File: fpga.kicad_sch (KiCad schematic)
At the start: 58 parts, among them J7 2X05, J8 61300411121, Q6 2N7002, U11 LIFCL-40-9BG256C, U17 SC18IS602BIPW, U18 W25Q32JVSSIQ, Y2 OSC40M-3.3_S5

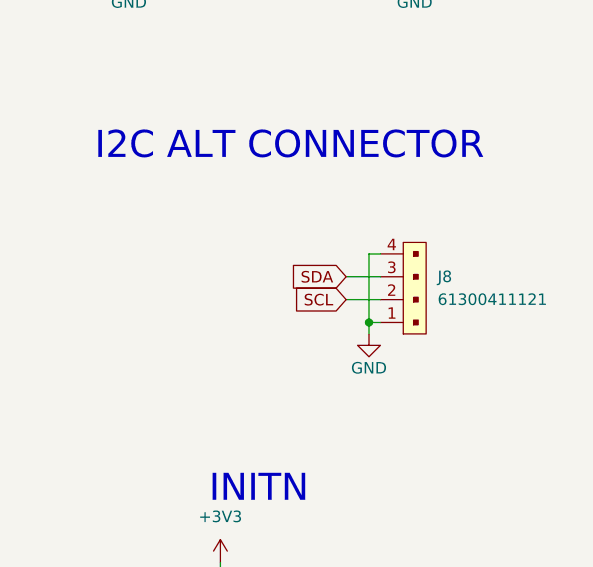
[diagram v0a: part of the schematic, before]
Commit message: Switched voltages to support DDR3 and RPC memories
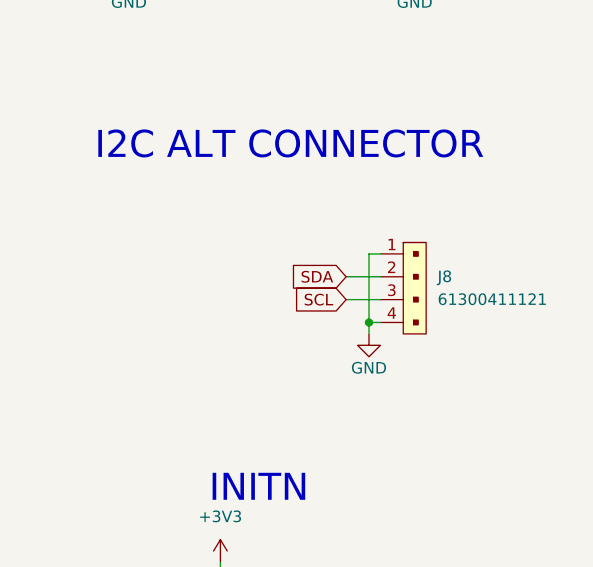
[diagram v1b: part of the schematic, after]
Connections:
- net SCL: now also J8.3; no longer J8.2
- net SDA: now also J8.2; no longer J8.3
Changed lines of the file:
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@@
     (pin "1")
   )
-  (symbol (lib_id "antmicroRectangularConnectorsHeadersMalePins:61300411121") (at 383.54 175.26 90) (unit 1)
+  (symbol (lib_id "antmicroRectangularConnectorsHeadersMalePins:61300411121") (at 383.54 167.64 90) (mirror x) (unit 1)
     (in_bom yes) (on_board yes) (fields_autoplaced)
     (property "Reference" "J8" (id 0) (at 386.08 170.1799 90)
@@
       (effects (font (size 1.27 1.27)) (justify right))
     )
-    (property "Footprint" "antmicro-footprints:PinHeader_1x4_P2.54mm_Drill1.02mm" (id 2) (at 378.46 170.18 0)
+    (property "Footprint" "antmicro-footprints:PinHeader_1x4_P2.54mm_Drill1.02mm" (id 2) (at 378.46 172.72 0)
       (effects (font (size 1.524 1.524)) (justify left) hide)
     )
-    (property "Datasheet" "" (id 3) (at 375.92 170.18 0)
+    (property "Datasheet" "" (id 3) (at 375.92 172.72 0)
       (effects (font (size 1.524 1.524)) (justify left) hide)
     )
-    (property "MPN" "61300411121" (id 4) (at 370.84 170.18 0)
+    (property "MPN" "61300411121" (id 4) (at 370.84 172.72 0)
       (effects (font (size 1.524 1.524)) (justify left) hide)
     )
-    (property "Manufacturer" "Wurth Electronics Inc." (id 5) (at 355.6 170.18 0)
+    (property "Manufacturer" "Wurth Electronics Inc." (id 5) (at 355.6 172.72 0)
       (effects (font (size 1.524 1.524)) (justify left) hide)
     )

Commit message: Placed components
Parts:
- C75: renamed from C81; value C_100n_0603 -> C_100n_0402; footprint crosslink-nx-video-converter-footprints:0603-cap -> antmicro-footprints:0402-cap; symbol crosslink-nx-video-converter:C_100n_0603 -> antmicroCapacitors0402:C_100n_0402; MPN 0603YC104KAZ2A -> GRM155R61H104KE14D; Manufacturer AVX -> Murata
- C79: renamed from C82; value C_100n_0603 -> C_100n_0402; footprint crosslink-nx-video-converter-footprints:0603-cap -> antmicro-footprints:0402-cap; symbol crosslink-nx-video-converter:C_100n_0603 -> antmicroCapacitors0402:C_100n_0402; DNP DNP -> (none); MPN 0603YC104KAZ2A -> GRM155R61H104KE14D; Manufacturer AVX -> Murata; now in the parts list
- C80: renamed from C83; value C_100n_0603 -> C_100n_0402; footprint crosslink-nx-video-converter-footprints:0603-cap -> antmicro-footprints:0402-cap; symbol crosslink-nx-video-converter:C_100n_0603 -> antmicroCapacitors0402:C_100n_0402; MPN 0603YC104KAZ2A -> GRM155R61H104KE14D; Manufacturer AVX -> Murata
- C81: renamed from C84; value C_100n_0603 -> C_100n_0402; footprint crosslink-nx-video-converter-footprints:0603-cap -> antmicro-footprints:0402-cap; symbol crosslink-nx-video-converter:C_100n_0603 -> antmicroCapacitors0402:C_100n_0402; MPN 0603YC104KAZ2A -> GRM155R61H104KE14D; Manufacturer AVX -> Murata
- C82: renamed from C85; value C_100n_0603 -> C_100n_0402; footprint crosslink-nx-video-converter-footprints:0603-cap -> antmicro-footprints:0402-cap; symbol crosslink-nx-video-converter:C_100n_0603 -> antmicroCapacitors0402:C_100n_0402; MPN 0603YC104KAZ2A -> GRM155R61H104KE14D; Manufacturer AVX -> Murata
- R39: renamed from R65; value R_0R_0603 -> R_0R_0402; footprint crosslink-nx-video-converter-footprints:0603-res -> antmicro-footprints:0402-res; symbol crosslink-nx-video-converter:R_0R_0603 -> antmicroResistors0402:R_0R_0402; DNP DNP -> (none); MPN CR0603-J/-000ELF -> ERJ2GE0R00X; Manufacturer BOURNS -> PANASONIC; now in the parts list
- R58: renamed from R66; value R_0R_0603 -> R_0R_0402; footprint crosslink-nx-video-converter-footprints:0603-res -> antmicro-footprints:0402-res; symbol crosslink-nx-video-converter:R_0R_0603 -> antmicroResistors0402:R_0R_0402; MPN CR0603-J/-000ELF -> ERJ2GE0R00X; Manufacturer BOURNS -> PANASONIC
- R65: renamed from R67; value R_0R_0603 -> R_0R_0402; footprint crosslink-nx-video-converter-footprints:0603-res -> antmicro-footprints:0402-res; symbol crosslink-nx-video-converter:R_0R_0603 -> antmicroResistors0402:R_0R_0402; MPN CR0603-J/-000ELF -> ERJ2GE0R00X; Manufacturer BOURNS -> PANASONIC
- R66: renamed from R69; value R_0R_0603 -> R_0R_0402; footprint crosslink-nx-video-converter-footprints:0603-res -> antmicro-footprints:0402-res; symbol crosslink-nx-video-converter:R_0R_0603 -> antmicroResistors0402:R_0R_0402; MPN CR0603-J/-000ELF -> ERJ2GE0R00X; Manufacturer BOURNS -> PANASONIC
- R67: renamed from R71; value R_0R_0603 -> R_0R_0402; footprint crosslink-nx-video-converter-footprints:0603-res -> antmicro-footprints:0402-res; symbol crosslink-nx-video-converter:R_0R_0603 -> antmicroResistors0402:R_0R_0402; MPN CR0603-J/-000ELF -> ERJ2GE0R00X; Manufacturer BOURNS -> PANASONIC
- R68, R81, R91: value R_10k_0603 -> R_10k_0402; footprint crosslink-nx-video-converter-footprints:0603-res -> antmicro-footprints:0402-res; symbol crosslink-nx-video-converter:R_10k_0603 -> antmicroResistors0402:R_10k_0402; MPN CR0603-JW-103ELF -> CRCW040210K0FKEDHP; Manufacturer BOURNS -> VISHAY
- R69: renamed from R73; value R_0R_0603 -> R_0R_0402; footprint crosslink-nx-video-converter-footprints:0603-res -> antmicro-footprints:0402-res; symbol crosslink-nx-video-converter:R_0R_0603 -> antmicroResistors0402:R_0R_0402; MPN CR0603-J/-000ELF -> ERJ2GE0R00X; Manufacturer BOURNS -> PANASONIC
- R70, R72, R84: value R_100R_0603 -> R_100R_0402; footprint crosslink-nx-video-converter-footprints:0603-res -> antmicro-footprints:0402-res; symbol crosslink-nx-video-converter:R_100R_0603 -> antmicroResistors0402:R_100R_0402; MPN MC0063W06035100R -> CR0402-FX-1000GLF; Manufacturer MULTICOMP -> BOURNS
- R71: renamed from R74; value R_0R_0603 -> R_0R_0402; footprint crosslink-nx-video-converter-footprints:0603-res -> antmicro-footprints:0402-res; symbol crosslink-nx-video-converter:R_0R_0603 -> antmicroResistors0402:R_0R_0402; MPN CR0603-J/-000ELF -> ERJ2GE0R00X; Manufacturer BOURNS -> PANASONIC
- R73: renamed from R75; value R_0R_0603 -> R_0R_0402; footprint crosslink-nx-video-converter-footprints:0603-res -> antmicro-footprints:0402-res; symbol crosslink-nx-video-converter:R_0R_0603 -> antmicroResistors0402:R_0R_0402; MPN CR0603-J/-000ELF -> ERJ2GE0R00X; Manufacturer BOURNS -> PANASONIC
- R74: renamed from R76; value R_0R_0603 -> R_0R_0402; footprint crosslink-nx-video-converter-footprints:0603-res -> antmicro-footprints:0402-res; symbol crosslink-nx-video-converter:R_0R_0603 -> antmicroResistors0402:R_0R_0402; MPN CR0603-J/-000ELF -> ERJ2GE0R00X; Manufacturer BOURNS -> PANASONIC
- R75: renamed from R77; value R_0R_0603 -> R_0R_0402; footprint crosslink-nx-video-converter-footprints:0603-res -> antmicro-footprints:0402-res; symbol crosslink-nx-video-converter:R_0R_0603 -> antmicroResistors0402:R_0R_0402; MPN CR0603-J/-000ELF -> ERJ2GE0R00X; Manufacturer BOURNS -> PANASONIC
- R76: renamed from R78; value R_0R_0603 -> R_0R_0402; footprint crosslink-nx-video-converter-footprints:0603-res -> antmicro-footprints:0402-res; symbol crosslink-nx-video-converter:R_0R_0603 -> antmicroResistors0402:R_0R_0402; MPN CR0603-J/-000ELF -> ERJ2GE0R00X; Manufacturer BOURNS -> PANASONIC
- R77: renamed from R80; value R_0R_0603 -> R_0R_0402; footprint crosslink-nx-video-converter-footprints:0603-res -> antmicro-footprints:0402-res; symbol crosslink-nx-video-converter:R_0R_0603 -> antmicroResistors0402:R_0R_0402; MPN CR0603-J/-000ELF -> ERJ2GE0R00X; Manufacturer BOURNS -> PANASONIC
- R78: renamed from R82; value R_0R_0603 -> R_0R_0402; footprint crosslink-nx-video-converter-footprints:0603-res -> antmicro-footprints:0402-res; symbol crosslink-nx-video-converter:R_0R_0603 -> antmicroResistors0402:R_0R_0402; MPN CR0603-J/-000ELF -> ERJ2GE0R00X; Manufacturer BOURNS -> PANASONIC
- R79: value R_1k_0603 -> R_1k_0402; footprint crosslink-nx-video-converter-footprints:0603-res -> antmicro-footprints:0402-res; symbol crosslink-nx-video-converter:R_1k_0603 -> antmicroResistors0402:R_1k_0402; MPN CR0603-JW-102ELF -> CR0402-FX-1001GLF
- R80: renamed from R85; value R_0R_0603 -> R_0R_0402; footprint crosslink-nx-video-converter-footprints:0603-res -> antmicro-footprints:0402-res; symbol crosslink-nx-video-converter:R_0R_0603 -> antmicroResistors0402:R_0R_0402; MPN CR0603-J/-000ELF -> ERJ2GE0R00X; Manufacturer BOURNS -> PANASONIC
- R82: renamed from R86; value R_0R_0603 -> R_0R_0402; footprint crosslink-nx-video-converter-footprints:0603-res -> antmicro-footprints:0402-res; symbol crosslink-nx-video-converter:R_0R_0603 -> antmicroResistors0402:R_0R_0402; MPN CR0603-J/-000ELF -> ERJ2GE0R00X; Manufacturer BOURNS -> PANASONIC
- R83, R87, R90: value R_4k7_0603 -> R_4k7_0402; footprint crosslink-nx-video-converter-footprints:0603-res -> antmicro-footprints:0402-res; symbol crosslink-nx-video-converter:R_4k7_0603 -> antmicroResistors0402:R_4k7_0402; MPN CR0603-FX-4701ELF -> MCS04020C4701FE000; Manufacturer BOURNS -> VISHAY
- R85: renamed from R88; value R_0R_0603 -> R_0R_0402; footprint crosslink-nx-video-converter-footprints:0603-res -> antmicro-footprints:0402-res; symbol crosslink-nx-video-converter:R_0R_0603 -> antmicroResistors0402:R_0R_0402; MPN CR0603-J/-000ELF -> ERJ2GE0R00X; Manufacturer BOURNS -> PANASONIC
- R86: renamed from R92; value R_0R_0603 -> R_0R_0402; footprint crosslink-nx-video-converter-footprints:0603-res -> antmicro-footprints:0402-res; symbol crosslink-nx-video-converter:R_0R_0603 -> antmicroResistors0402:R_0R_0402; MPN CR0603-J/-000ELF -> ERJ2GE0R00X; Manufacturer BOURNS -> PANASONIC
- R88: renamed from R94; value R_0R_0603 -> R_0R_0402; footprint crosslink-nx-video-converter-footprints:0603-res -> antmicro-footprints:0402-res; symbol crosslink-nx-video-converter:R_0R_0603 -> antmicroResistors0402:R_0R_0402; MPN CR0603-J/-000ELF -> ERJ2GE0R00X; Manufacturer BOURNS -> PANASONIC
- R89, R93: value R_2k2_0603 -> R_2k2_0402; footprint crosslink-nx-video-converter-footprints:0603-res -> antmicro-footprints:0402-res; symbol crosslink-nx-video-converter:R_2k2_0603 -> antmicroResistors0402:R_2k2_0402; MPN MCMR06X2201FTL -> RC0402FR-072K2L; Manufacturer MULTICOMP -> YAGEO
- R92: renamed from R95; value R_0R_0603 -> R_0R_0402; footprint crosslink-nx-video-converter-footprints:0603-res -> antmicro-footprints:0402-res; symbol crosslink-nx-video-converter:R_0R_0603 -> antmicroResistors0402:R_0R_0402; MPN CR0603-J/-000ELF -> ERJ2GE0R00X; Manufacturer BOURNS -> PANASONIC
- R94: renamed from R96; value R_0R_0603 -> R_0R_0402; footprint crosslink-nx-video-converter-footprints:0603-res -> antmicro-footprints:0402-res; symbol crosslink-nx-video-converter:R_0R_0603 -> antmicroResistors0402:R_0R_0402; MPN CR0603-J/-000ELF -> ERJ2GE0R00X; Manufacturer BOURNS -> PANASONIC
- R95: renamed from R97; value R_0R_0603 -> R_0R_0402; footprint crosslink-nx-video-converter-footprints:0603-res -> antmicro-footprints:0402-res; symbol crosslink-nx-video-converter:R_0R_0603 -> antmicroResistors0402:R_0R_0402; MPN CR0603-J/-000ELF -> ERJ2GE0R00X; Manufacturer BOURNS -> PANASONIC
- R96: renamed from R98; value R_0R_0603 -> R_0R_0402; footprint crosslink-nx-video-converter-footprints:0603-res -> antmicro-footprints:0402-res; symbol crosslink-nx-video-converter:R_0R_0603 -> antmicroResistors0402:R_0R_0402; MPN CR0603-J/-000ELF -> ERJ2GE0R00X; Manufacturer BOURNS -> PANASONIC
- R97: renamed from R99; value R_10k_0603 -> R_10k_0402; footprint crosslink-nx-video-converter-footprints:0603-res -> antmicro-footprints:0402-res; symbol crosslink-nx-video-converter:R_10k_0603 -> antmicroResistors0402:R_10k_0402; MPN CR0603-JW-103ELF -> CRCW040210K0FKEDHP; Manufacturer BOURNS -> VISHAY
- TP15: renamed from TP16; value TP -> TP_SMD_0_75MM; footprint crosslink-nx-video-converter-footprints:TP-R-1.5 -> antmicro-footprints:Testpoint_smd_0_75mm; symbol crosslink-nx-video-converter:TP -> antmicroTestPoints:TP_SMD_0_75MM
- TP16: renamed from TP17; value TP -> TP_SMD_0_75MM; footprint crosslink-nx-video-converter-footprints:TP-R-1.5 -> antmicro-footprints:Testpoint_smd_0_75mm; symbol crosslink-nx-video-converter:TP -> antmicroTestPoints:TP_SMD_0_75MM
- TP17: renamed from TP18; value TP -> TP_SMD_0_75MM; footprint crosslink-nx-video-converter-footprints:TP-R-1.5 -> antmicro-footprints:Testpoint_smd_0_75mm; symbol crosslink-nx-video-converter:TP -> antmicroTestPoints:TP_SMD_0_75MM
- TP18: renamed from TP19; value TP -> TP_SMD_0_75MM; footprint crosslink-nx-video-converter-footprints:TP-R-1.5 -> antmicro-footprints:Testpoint_smd_0_75mm; symbol crosslink-nx-video-converter:TP -> antmicroTestPoints:TP_SMD_0_75MM
- TP19: renamed from TP20; value TP -> TP_SMD_0_75MM; footprint crosslink-nx-video-converter-footprints:TP-R-1.5 -> antmicro-footprints:Testpoint_smd_0_75mm; symbol crosslink-nx-video-converter:TP -> antmicroTestPoints:TP_SMD_0_75MM
- TP20: renamed from TP21; value TP -> TP_SMD_0_75MM; footprint crosslink-nx-video-converter-footprints:TP-R-1.5 -> antmicro-footprints:Testpoint_smd_0_75mm; symbol crosslink-nx-video-converter:TP -> antmicroTestPoints:TP_SMD_0_75MM
- TP21: renamed from TP22; value TP -> TP_SMD_0_75MM; footprint crosslink-nx-video-converter-footprints:TP-R-1.5 -> antmicro-footprints:Testpoint_smd_0_75mm; symbol crosslink-nx-video-converter:TP -> antmicroTestPoints:TP_SMD_0_75MM
- TP22: renamed from TP23; value TP -> TP_SMD_0_75MM; footprint crosslink-nx-video-converter-footprints:TP-R-1.5 -> antmicro-footprints:Testpoint_smd_0_75mm; symbol crosslink-nx-video-converter:TP -> antmicroTestPoints:TP_SMD_0_75MM

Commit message: Loclib
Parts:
- C75, C79, C80, C81, C82: footprint antmicro-footprints:0402-cap -> crosslink-nx-video-converter-footprints:0402-cap; symbol antmicroCapacitors0402:C_100n_0402 -> crosslink-nx-video-converter:C_100n_0402
- J8: footprint antmicro-footprints:PinHeader_1x4_P2.54mm_Drill1.02mm -> crosslink-nx-video-converter-footprints:PinHeader_1x4_P2.54mm_Drill1.02mm; symbol antmicroRectangularConnectorsHeadersMalePins:61300411121 -> crosslink-nx-video-converter:61300411121
- R39, R58, R65, R66, R67, R69, R71, R73, R74, R75, R76, R77, R78, R80, R82, R85, R86, R88, R92, R94, R95, R96: footprint antmicro-footprints:0402-res -> crosslink-nx-video-converter-footprints:0402-res; symbol antmicroResistors0402:R_0R_0402 -> crosslink-nx-video-converter:R_0R_0402
- R68, R81, R91, R97: footprint antmicro-footprints:0402-res -> crosslink-nx-video-converter-footprints:0402-res; symbol antmicroResistors0402:R_10k_0402 -> crosslink-nx-video-converter:R_10k_0402
- R70, R72, R84: footprint antmicro-footprints:0402-res -> crosslink-nx-video-converter-footprints:0402-res; symbol antmicroResistors0402:R_100R_0402 -> crosslink-nx-video-converter:R_100R_0402
- R79: footprint antmicro-footprints:0402-res -> crosslink-nx-video-converter-footprints:0402-res; symbol antmicroResistors0402:R_1k_0402 -> crosslink-nx-video-converter:R_1k_0402
- R83, R87, R90: footprint antmicro-footprints:0402-res -> crosslink-nx-video-converter-footprints:0402-res; symbol antmicroResistors0402:R_4k7_0402 -> crosslink-nx-video-converter:R_4k7_0402
- R89, R93: footprint antmicro-footprints:0402-res -> crosslink-nx-video-converter-footprints:0402-res; symbol antmicroResistors0402:R_2k2_0402 -> crosslink-nx-video-converter:R_2k2_0402
- TP15, TP16, TP17, TP18, TP19, TP20, TP21, TP22: footprint antmicro-footprints:Testpoint_smd_0_75mm -> crosslink-nx-video-converter-footprints:Testpoint_smd_0_75mm; symbol antmicroTestPoints:TP_SMD_0_75MM -> crosslink-nx-video-converter:TP_SMD_0_75MM
- U11: footprint antmicro-footprints:BGA-256_16x16_14.0x14.0mm -> crosslink-nx-video-converter-footprints:BGA-256_16x16_14.0x14.0mm; symbol antmicroBGAchips:LIFCL-40-9BG256C -> crosslink-nx-video-converter:LIFCL-40-9BG256C
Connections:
- net +3V3: no longer U11.D13 (VCCIO0)
- net DONE: no longer U11.B16 (PT76B/DONE )
- net GND: no longer U11.A14 (SD0_RXDN), U11.A15 (SD0_RXDP), U11.A9 (SD_REFCLKP), U11.B9 (SD_REFCLKN), U11.C11 (SD0_REXT)
- net INITN: no longer U11.D11 (PT74A/INITN )
- net LED0: no longer U11.E15 (PT84A)
- net LED1: no longer U11.E16 (PT84B)
- net PROGRAMN: no longer U11.C12 (PT74B/PROGRAMN)
- net SPI_CLK: no longer U11.C16 (PT76A/MCLK/PCLKT0_0)
- net SPI_DQ0_MOSI: no longer U11.C14 (PT78B/MOSI/MD0)
- net SPI_DQ1_MISO: no longer U11.D16 (PT80A/MISO/MD1)
- net SPI_DQ2: no longer U11.D15 (PT80B/MD2)
- net SPI_DQ3: no longer U11.D12 (PT82A/MD3)
- net ~{FLASH_CS}: no longer U11.C15 (PT78A/MCSN/PCLKT0_1)

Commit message: Routed hard CSI
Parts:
- removed unit 1 of U11
- removed unit 12 of U11
- added unit 12 of U11
- added unit 1 of U11
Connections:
- net +3V3: now also U11.D13 (VCCIO0)
- net DONE: now also U11.B16 (PT76B/DONE )
- net GND: now also U11.A14 (SD0_RXDN), U11.A15 (SD0_RXDP), U11.A9 (SD_REFCLKP), U11.B9 (SD_REFCLKN), U11.C11 (SD0_REXT)
- net INITN: now also U11.D11 (PT74A/INITN )
- net LED0: now also U11.E15 (PT84A)
- net LED1: now also U11.E16 (PT84B)
- net PROGRAMN: now also U11.C12 (PT74B/PROGRAMN)
- net SPI_CLK: now also U11.C16 (PT76A/MCLK/PCLKT0_0)
- net SPI_DQ0_MOSI: now also U11.C14 (PT78B/MOSI/MD0)
- net SPI_DQ1_MISO: now also U11.D16 (PT80A/MISO/MD1)
- net SPI_DQ2: now also U11.D15 (PT80B/MD2)
- net SPI_DQ3: now also U11.D12 (PT82A/MD3)
- net ~{FLASH_CS}: now also U11.C15 (PT78A/MCSN/PCLKT0_1)

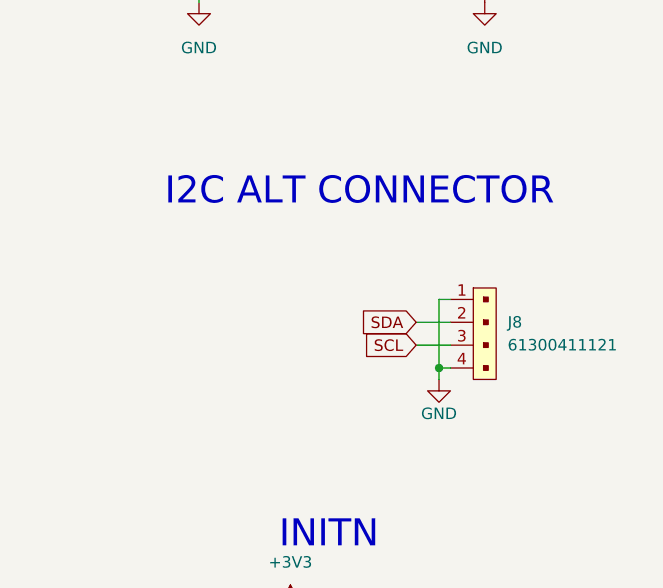
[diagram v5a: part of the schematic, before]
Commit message: Added QWIIC connector
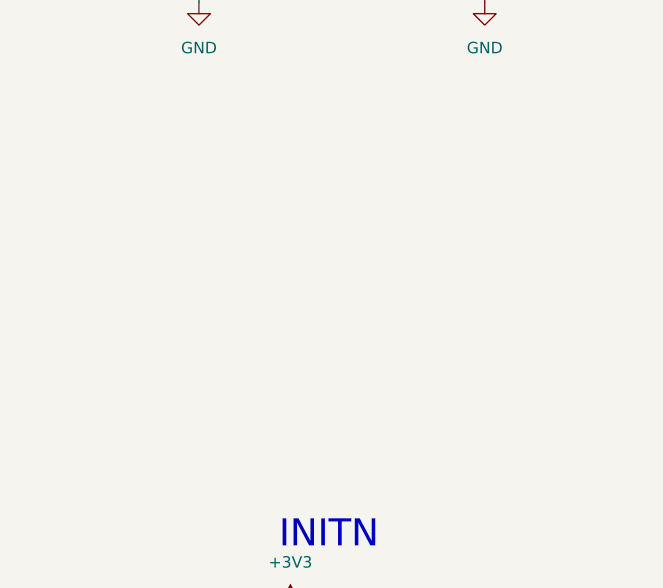
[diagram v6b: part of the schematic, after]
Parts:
- removed J8: 61300411121, crosslink-nx-video-converter-footprints:PinHeader_1x4_P2.54mm_Drill1.02mm, symbol crosslink-nx-video-converter:61300411121
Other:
- note removed: "I2C ALT CONNECTOR"
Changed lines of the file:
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@@
   (junction (at 293.37 142.24) (diameter 0) (color 0 0 0 0)
-  )
-  (junction (at 378.46 175.26) (diameter 0) (color 0 0 0 0)
   )
   (junction (at 140.97 151.13) (diameter 0) (color 0 0 0 0)
@@
     (stroke (width 0) (type default) (color 0 0 0 0))
   )
-  (wire (pts (xy 378.46 167.64) (xy 378.46 175.26))
-    (stroke (width 0) (type default) (color 0 0 0 0))
-  )
-  (wire (pts (xy 379.73 167.64) (xy 378.46 167.64))
-    (stroke (width 0) (type default) (color 0 0 0 0))
-  )
   (polyline (pts (xy 120.65 219.71) (xy 120.65 284.48))
     (stroke (width 0) (type default) (color 0 0 0 0))
@@
     (stroke (width 0) (type default) (color 0 0 0 0))
   )
-  (wire (pts (xy 378.46 175.26) (xy 378.46 176.53))
-    (stroke (width 0) (type default) (color 0 0 0 0))
-  )
   (wire (pts (xy 351.79 115.57) (xy 354.33 115.57))
     (stroke (width 0) (type default) (color 0 0 0 0))
@@
     (stroke (width 0) (type default) (color 0 0 0 0))
   )
-  (wire (pts (xy 375.92 172.72) (xy 379.73 172.72))
-    (stroke (width 0) (type default) (color 0 0 0 0))
-  )
   (wire (pts (xy 317.5 48.26) (xy 317.5 60.96))
     (stroke (width 0) (type default) (color 0 0 0 0))
@@
     (stroke (width 0) (type default) (color 0 0 0 0))
   )
-  (wire (pts (xy 375.92 170.18) (xy 379.73 170.18))
-    (stroke (width 0) (type default) (color 0 0 0 0))
-  )
   (wire (pts (xy 262.89 60.96) (xy 297.18 60.96))
     (stroke (width 0) (type default) (color 0 0 0 0))
@@
   )
   (wire (pts (xy 351.79 123.19) (xy 351.79 134.62))
-    (stroke (width 0) (type default) (color 0 0 0 0))
-  )
-  (wire (pts (xy 378.46 175.26) (xy 379.73 175.26))
     (stroke (width 0) (type default) (color 0 0 0 0))
   )
@@
   )
   (text "INITN" (at 360.68 195.58 0)
-    (effects (font (size 3 3)) (justify left bottom))
-  )
-  (text "I2C ALT CONNECTOR" (at 347.98 157.48 0)
     (effects (font (size 3 3)) (justify left bottom))
   )
@@
     )
   )
-  (global_label "SDA" (shape input) (at 375.92 170.18 180) (fields_autoplaced)
-    (effects (font (size 1.27 1.27)) (justify right))
-    (property "Intersheet References" "${INTERSHEET_REFS}" (id 0) (at 369.9388 170.1006 0)
-      (effects (font (size 1.27 1.27)) (justify right) hide)
-    )
-  )
-  (global_label "SCL" (shape input) (at 375.92 172.72 180) (fields_autoplaced)
-    (effects (font (size 1.27 1.27)) (justify right))
-    (property "Intersheet References" "${INTERSHEET_REFS}" (id 0) (at 369.9993 172.6406 0)
-      (effects (font (size 1.27 1.27)) (justify right) hide)
-    )
-  )
   (symbol (lib_id "crosslink-nx-video-converter:C_100n_0402") (at 354.33 46.99 0) (unit 1)
     (in_bom yes) (on_board yes)
@@
     )
     (pin "1")
-  )
-  (symbol (lib_id "crosslink-nx-video-converter:61300411121") (at 383.54 167.64 90) (mirror x) (unit 1)
-    (in_bom yes) (on_board yes) (fields_autoplaced)
-    (property "Reference" "J8" (id 0) (at 386.08 170.1799 90)
-      (effects (font (size 1.27 1.27)) (justify right))
-    )
-    (property "Value" "61300411121" (id 1) (at 386.08 172.7199 90)
-      (effects (font (size 1.27 1.27)) (justify right))
-    )
-    (property "Footprint" "crosslink-nx-video-converter-footprints:PinHeader_1x4_P2.54mm_Drill1.02mm" (id 2) (at 378.46 172.72 0)
-      (effects (font (size 1.524 1.524)) (justify left) hide)
-    )
-    (property "Datasheet" "" (id 3) (at 375.92 172.72 0)
-      (effects (font (size 1.524 1.524)) (justify left) hide)
-    )
-    (property "MPN" "61300411121" (id 4) (at 370.84 172.72 0)
-      (effects (font (size 1.524 1.524)) (justify left) hide)
-    )
-    (property "Manufacturer" "Wurth Electronics Inc." (id 5) (at 355.6 172.72 0)
-      (effects (font (size 1.524 1.524)) (justify left) hide)
-    )
-    (pin "1")
-    (pin "2")
-    (pin "3")
-    (pin "4")
   )
   (symbol (lib_id "crosslink-nx-video-converter:R_0R_0402") (at 299.72 236.22 0) (unit 1)
@@
       (effects (font (size 1.27 1.27)) hide)
     )
-    (pin "1")
-  )
-  (symbol (lib_id "crosslink-nx-video-converter:GND") (at 378.46 176.53 0) (unit 1)
-    (in_bom yes) (on_board yes)
-    (property "Reference" "#PWR0185" (id 0) (at 378.46 182.88 0)
-      (effects (font (size 1.27 1.27)) hide)
-    )
-    (property "Value" "GND" (id 1) (at 378.46 180.34 0))
-    (property "Footprint" "crosslink-nx-video-converter-footprints:" (id 2) (at 378.46 176.53 0)
-      (effects (font (size 1.27 1.27)) hide)
-    )
-    (property "Datasheet" "" (id 3) (at 378.46 176.53 0)
-      (effects (font (size 1.27 1.27)) hide)
-    )
